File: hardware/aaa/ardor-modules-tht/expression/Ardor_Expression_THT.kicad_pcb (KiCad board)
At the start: 2 copper layers, 110 x 85 mm, 31 parts, among them J101 3V3 POWER INPUT + I2C TO HOST, J302 PASSIVE PEDAL INPUT / EXCITAT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, U301 Adafruit 1085 ADS1115 QT

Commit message: fix(hardware): use Hestore TVS diodes in hand-assembly modules
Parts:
- D301, D302: value SA5.0CA-E3/54 -> 1.5KE6.8CA; footprint Diode_THT:D_DO-15_P10.16mm_Horizontal -> Ardor_THT:D_TVS_DC_1.5KE_P15.24mm
- moved D301 2.54 mm to (54.9, 67.5)
- moved D302 2.54 mm to (54.9, 97.5)
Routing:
- net Net-(JP301-Pin_3): track 26.0 -> 32.7 mm
- net Net-(D303-A): track 59.2 -> 53.0 mm
- net /+3V3_A: track 174.0 -> 175.1 mm
- net /EXP_TIP: track 35.0 -> 36.1 mm
- net /EXP_RING: track 39.4 -> 40.2 mm
- net Net-(D305-A): track 48.8 -> 48.3 mm

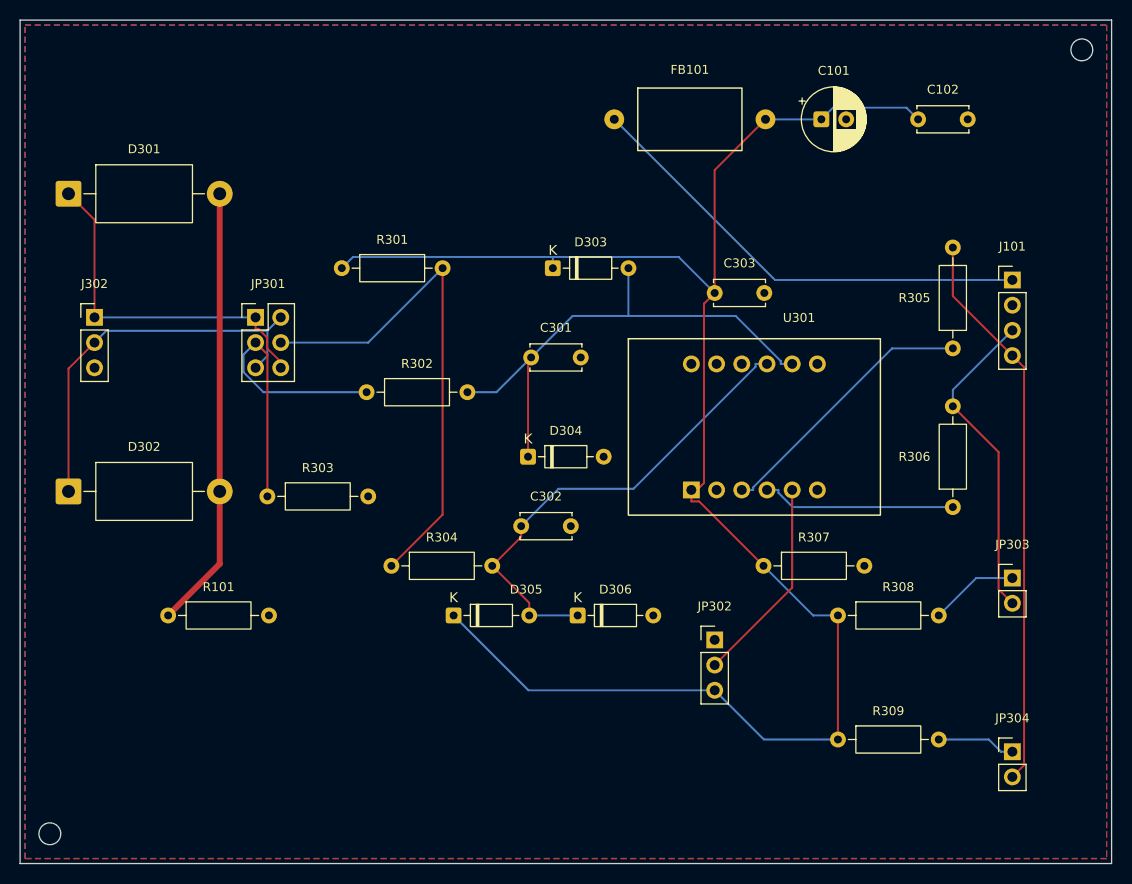
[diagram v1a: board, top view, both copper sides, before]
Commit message: feat(hardware): compact layouts and adopt Hestore module packages
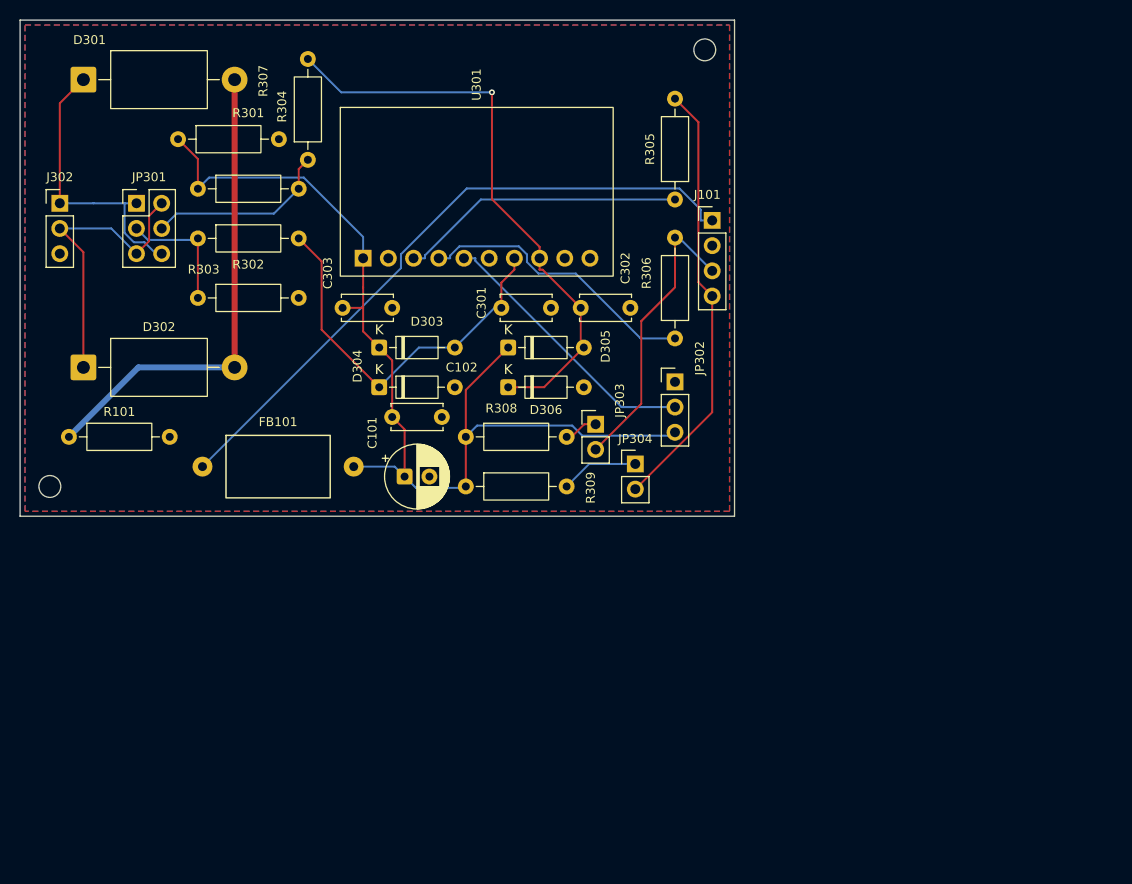
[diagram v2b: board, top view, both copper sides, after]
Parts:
- U301: value Adafruit 1085 ADS1115 QT -> ADS1115-M; footprint Ardor_THT:Adafruit_ADS1115_1085_STEMMA_QT -> Ardor_THT:ADS1115_M_HESTORE_10041798
- moved R307 73.0 mm to (65.9, 62.0)
- moved C102 60.9 mm to (87.5, 90.0)
- moved C101 55.3 mm to (88.8, 96.0)
- moved FB101 54.3 mm to (68.4, 95.0)
- moved JP304 47.8 mm to (112.0, 94.7)
- moved R309 45.3 mm to (94.9, 97.0)
- moved JP303 44.8 mm to (108.0, 90.7)
- moved R304 41.8 mm to (79.0, 64.1), turned to 90 degrees
- moved R308 41.6 mm to (94.9, 92.0)
- moved H2 38.0 mm to (119.0, 53.0)
- moved C303 37.5 mm to (82.5, 79.0)
- moved H1 35.0 mm to (53.0, 97.0)
- moved R306 32.8 mm to (116.0, 82.1)
- moved U301 32.8 mm to (96.0, 74.0)
- moved R305 31.8 mm to (116.0, 68.1)
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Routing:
- net /+3V3_A: track 175.1 -> 103.5 mm
- net /EXP_EXC: track 51.6 -> 18.8 mm
- net Net-(JP301-Pin_3): track 32.7 -> 12.7 mm
- net /+3V3: track 46.8 -> 65.8 mm
- net Net-(D303-A): track 53.0 -> 39.5 mm
- net /SCL: track 56.8 -> 44.1 mm
- net Net-(D305-A): track 48.3 -> 59.0 mm, vias 0 -> 1
- net /EXP_RING: track 40.2 -> 29.9 mm
- net Net-(U301-SDA): track 19.6 -> 28.8 mm
- net /EXP_TIP: track 36.1 -> 28.8 mm
- net Net-(JP302-Pin_2): track 20.9 -> 27.6 mm
- net Net-(JP303-Pin_1): track 8.98 -> 3.45 mm
- net /CHASSIS: track 44.7 -> 48.6 mm
- net /SDA: track 32.5 -> 29.8 mm
- net Net-(U301-SCL): track 27.3 -> 29.0 mm
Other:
- board size 110 x 85 mm -> 72 x 50 mm
- board text removed: "U301.11 NC NO WIRE"
- board text removed: "U301.12 NC NO WIRE"
